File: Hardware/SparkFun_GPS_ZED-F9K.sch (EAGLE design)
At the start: 31 parts, among them J4 U.FL, Y1 32.768kHz

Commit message: Adds circuitry for active antenna or RF_IN
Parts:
- removed FRAME1: FRAME-LETTER, SparkFun-Aesthetics:FRAME-LETTER
- removed L2: 2.2uH, SparkFun-Coils:2.2μH_SHIELDED_INDUCTOR
- removed Y1: 32.768kHz, SparkFun-Clocks:CRYSTAL-32.768KHZSMD-3.2X1.5
- added D3: 24V, SparkFun-DiscreteSemi:DIODE_TVS
- added FRAME2: FRAME-LEDGER, SparkFun-Aesthetics:FRAME-LEDGER
- added J2: (no value), SparkFun-Connectors:USB_C2-LAYER
- added L1: 3.9NH, SparkFun-Coils:INDUCTOR-0402-3.9NH
- added Q1, Q2: 600mA/40V, SparkFun-DiscreteSemi:TRANS_PNP-MMBT4403
- added R6: 22, SparkFun-Resistors:22OHM-0402-1/10W-1%
- added R7: 10, SparkFun-Resistors:10OHM-0603-1/10W-5%
- added U1: UBLOX_ZED_F9K, classified:UBLOX_ZED_F9K
- C1: value 4.7uF -> 0.1uF; device SparkFun-Capacitors:4.7UF-0603-6.3V-(10%) -> SparkFun-Capacitors:0.1UF-0402-16V-10%
- C2: value 0.1uF -> 1.0uF; device SparkFun-Capacitors:0.1UF-0603-25V-(+80/-20%) -> SparkFun-Capacitors:1.0UF-0402-16V-10%
- FB1: value FERRITE_BEAD-120_OHM-0402 -> FERRITE_BEAD; device SparkFun-Coils:FERRITE_BEAD-120_OHM-0402 -> SparkFun-Coils:FERRITE_BEAD
- R5: value 10 -> 2.2KOHM-0402-1/16W-1%; device SparkFun-Resistors:10OHM-0603-1/10W-1% -> SparkFun-Resistors:2.2KOHM-0402-1/16W-1%
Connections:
- removed net ANT: FB1.1, J4.SIGNAL
- new net N$10: C1.1, L1.1, Q1.E
- new net N$11: Q2.E, R6.1
- new net N$5: C2.2, FB1.2, R6.2, R7.1
- new net N$6: Q1.B, Q2.C, R5.1
- new net N$7: C3.2, D3.C, J4.SIGNAL, L1.2
- new net RF_IN: C3.1, U1.RF_IN
- net 3.3V: now also FB1.1, U1.VCC; no longer R5.2
- net GND: now also C1.2, C2.1, D3.A, R5.2, U1.GND; no longer C3.2
- net N$9: now also Q1.C, Q2.B, R7.2; no longer C3.1, FB1.2, R5.1
- net V_BATT: now also U1.V_BKCP
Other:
- note added: "2.2K Ohm"
- note added: "VCC Range: 2.7V - 3.6V"
- note added: "ublox ZED-F9P"
- note added: "v01"
- note removed: "VCC Range: 1.89 - 3.6V"
- note removed: "uBlox ZOE-M8Q-0-10"
- note removed: "v10"
- moved on the sheet: B1, C1, C2, C3, D1, D2, FB1, J1, J3, J4, J5, JP1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

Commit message: Adds power circuitry with ESD protection, adds LEDs
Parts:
- removed JP4: JUMPER-SMT_2_NC_TRACE_SILK, SparkFun-Jumpers:JUMPER-SMT_2_NC_TRACE_SILK
- added C4, C5: 1.0uF, SparkFun-Capacitors:1.0UF-0603-16V-10%-X7R
- added C6: 1.0uF, SparkFun-Capacitors:1.0UF-0402-16V-10%
- added D4: PRTR5V0U2F, SparkFun-IC-Power:PRTR5V0U2F
- added D5, D6: BLUE, SparkFun-LED:LED-BLUE0603
- added J6: QWIIC_RIGHT_ANGLE, SparkFun-Connectors:QWIIC_CONNECTORJS-1MM
- added PPS, PWR, RTK: JUMPER-SMT_2_NC_TRACE_SILK, SparkFun-Jumpers:JUMPER-SMT_2_NC_TRACE_SILK
- added R10, R11: 27, SparkFun-Resistors:27OHM-0603-1/10W-1%
- added R12: 100K, SparkFun-Resistors:100KOHM-0402-1/16W-1%
- added R13, R14: 1KOHM-0402-1/16W-1%, SparkFun-Resistors:1KOHM-0402-1/16W-1%
- added R8, R9: 5.1k, SparkFun-Resistors:5.1KOHM5.1KOHM-0603-1/10W-1%
- added U2: 3.3V, SparkFun-IC-Power:V_REG_AP2112K-3.3V
- J1: value (none) -> QWIIC_RIGHT_ANGLE
- J5: device SparkFun-Connectors:CONN_041X04_NO_SILK -> SparkFun-Connectors:CONN_07
- R3, R4: value 2.2k -> 2.2K; device SparkFun-Resistors:2.2KOHM-0603-1/10W-1% -> SparkFun-Resistors:2.2KOHM-0402-1/16W-1%
- R5: value 2.2KOHM-0402-1/16W-1% -> 2.2K
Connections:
- removed net SDA/CS: J1.3, J3.8, R3.1
- removed net TIMEPULSE: J5.3
- new net DIR: J5.7, U1.DIR
- new net DMINUS: R11.2, U1.USB_D-
- new net DPLUS: R10.2, U1.USB_D+
- new net INT: U1.EXTINT
- new net N$14: J2.CC2, R8.2
- new net N$15: J2.CC1, R9.2
- new net N$16: D4.5, R10.1
- new net N$17: D4.4, R11.1
- new net N$20: D4.2, J2.D+
- new net N$21: D4.3, J2.D-
- new net N$22: R14.1, RTK.2
- new net N$23: PPS.2, R13.1
- new net N$24: D5.C, R13.2
- new net N$25: D6.C, R14.2
- new net PPS: D5.A, J5.3, U1.TIMEPULSE
- new net RTK_STAT: D6.A, U1.RTK_STAT
- new net RXI2: U1.RX2
- new net SDA/!CS: J1.3, J3.8, J6.3, R3.1, U1.SDA/!CS!
- new net SHLD: J2.SHLD
- new net TXO2: U1.TX2
- new net TX_READY: J5.5, U1.TX_READY
- new net VIN: D4.1, J2.VBUS, J3.4
- new net VOUT: C4.1, D4.6, U2.EN, U2.IN
- new net WT: J5.6, U1.WHEEL_TKS
- net !RESET: now also U1.!RESET!
- net !SAFEBOOT: now also U1.!SAFEBOOT!
- net 3.3V: now also C5.1, C6.1, D2.A, J6.2, R12.2, U1.V_USB, U2.OUT; no longer J3.4, R2.2
- net D_SEL: now also U1.D_SEL
- net GND: now also C4.2, C5.2, C6.2, J2.GND, J6.1, PPS.1, PWR.1, R12.1, R8.1, R9.1, RTK.1, U2.GND; no longer JP4.1
- net N$4: now also D2.C, R2.2; no longer D2.A, R2.1
- net N$8: now also PWR.2, R2.1; no longer D2.C, JP4.2
- net RXI/MOSI: now also U1.RX/MOSI
- net SCL/CLK: now also J6.4, U1.SCL/CLK
- net TXO/MISO: now also U1.TX/MISO
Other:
- note added: "!!!"
- note added: "1k"
- note added: "ADR Module - ublox ZED-F9P"
- note added: "Cut trace to disconnect respective LED"
- note added: "Order new parts"
- note added: "Power"
- note added: "VIN Range: 2.5V - 6V Max Current: 600mA"
- note removed: "Cut trace to disconnect LED"
- note removed: "ublox ZED-F9P"
- moved on the sheet: B1, C1, C2, C3, D1, D2, D3, FB1, J1, J2, J3, J4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

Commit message: Adds I/O protection to INPUTS using new part, removes active antenna circuitry in place of VCC bias for external patch active antennas
* Localizes parts into a rough shape for final product
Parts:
- removed C2: 1.0uF, SparkFun-Capacitors:1.0UF-0402-16V-10%
- removed C3: 47pF, SparkFun-Capacitors:47PF-0603-50V-5%
- removed D3: 24V, SparkFun-DiscreteSemi:DIODE_TVS
- removed FB1: FERRITE_BEAD, SparkFun-Coils:FERRITE_BEAD
- removed LOGO1: SFE_LOGO_NAME_FLAME.1_INCH, SparkFun-Aesthetics:SFE_LOGO_NAME_FLAME.1_INCH
- removed LOGO2: OSHW-LOGOS, SparkFun-Aesthetics:OSHW-LOGOS
- removed LOGO3: SFE_LOGO_FLAME.1_INCH, SparkFun-Aesthetics:SFE_LOGO_FLAME.1_INCH
- removed Q1, Q2: 600mA/40V, SparkFun-DiscreteSemi:TRANS_PNP-MMBT4403
- removed R6: 22, SparkFun-Resistors:22OHM-0402-1/10W-1%
- removed R7: 10, SparkFun-Resistors:10OHM-0603-1/10W-5%
- added U3: TRIPLE_BUFFER_74LVC3G07, classified:TRIPLE_BUFFER_74LVC3G07
- J5: device SparkFun-Connectors:CONN_07 -> SparkFun-Connectors:CONN_07NO_SILK
- L1: device SparkFun-Coils:INDUCTOR-0402-3.9NH -> SparkFun-Coils:FERRITE_BEAD-120_OHM-0402
- R5: value 2.2K -> 20; device SparkFun-Resistors:2.2KOHM-0402-1/16W-1% -> SparkFun-Resistors:20OHM-0603-1/10W-1%
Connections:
- removed net !INT: J5.1
- removed net !RESET: J5.2, U1.!RESET!
- removed net !SAFEBOOT: J5.4, U1.!SAFEBOOT!
- removed net INT: U1.EXTINT
- removed net N$10: C1.1, L1.1, Q1.E
- removed net N$11: Q2.E, R6.1
- removed net N$20: D4.2, J2.D+
- removed net N$21: D4.3, J2.D-
- removed net N$9: Q1.C, Q2.B, R7.2
- removed net VOUT: C4.1, D4.6, U2.EN, U2.IN
- new net !RESET_IN: U1.!RESET!, U3.1A
- new net !RESET_OUT: J5.2, U3.1Y
- new net !SAFEBOOT_IN: U1.!SAFEBOOT!, U3.3A
- new net !SAFEBOOT_OUT: J5.4, U3.3Y
- new net INT_IN: U1.EXTINT, U3.2A
- new net INT_OUT: J5.1, U3.2Y
- new net V_RF: R5.2, U1.V_RF
- new net V_USB: D4.1, J2.VBUS
- net 3.3V: now also U3.VCC; no longer FB1.1
- net DMINUS: now also R10.2; no longer R11.2
- net DPLUS: now also R11.2; no longer R10.2
- net GND: now also U3.GND; no longer C2.1, D3.A, R5.2
- net N$5: now also C1.1, L1.2, R5.1; no longer C2.2, FB1.2, R6.2, R7.1
- net N$6: now also D4.3, J2.D+; no longer Q1.B, Q2.C, R5.1
- net N$7: now also D4.2, J2.D-; no longer C3.2, D3.C, J4.SIGNAL, L1.2
- net RF_IN: now also J4.SIGNAL, L1.1; no longer C3.1
- net VIN: now also C4.1, D4.6, U2.EN, U2.IN; no longer D4.1, J2.VBUS
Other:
- note added: "I/O Buffer"
- note removed: "2.2K Ohm"
- moved on the sheet: C1, J3, J4, J5, R5

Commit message: Solidifies breakout board size
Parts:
- added J8: (no value), SparkFun-Connectors:CONN_09NO_SILK
- J3: device SparkFun-Connectors:CONN_08NO_SILK_FEMALE_PTH -> SparkFun-Connectors:CONN_06NO_SILK_NO_POP
- J5: device SparkFun-Connectors:CONN_07NO_SILK -> SparkFun-Connectors:CONN_06NO_SILK_NO_POP
- R2: value 1k -> 1KOHM-0402-1/16W-1%; device SparkFun-Resistors:1KOHM-0603-1/10W-1% -> SparkFun-Resistors:1KOHM-0402-1/16W-1%
- R8, R9: device SparkFun-Resistors:5.1KOHM5.1KOHM-0603-1/10W-1% -> SparkFun-Resistors:5.1KOHM-0402-1/16W-1%
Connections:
- new net !CS: J3.3
- new net SCK: J3.6
- net !RESET_OUT: now also J8.2; no longer J5.2
- net !SAFEBOOT_IN: now also J8.3
- net !SAFEBOOT_OUT: no longer J5.4
- net 3.3V: now also J8.7
- net DIR: no longer J5.7
- net GND: now also J3.1, J5.1, J8.6; no longer J3.6
- net INT_OUT: now also J8.4; no longer J5.1
- net PPS: now also J8.1; no longer J5.3
- net RXI/MOSI: now also J3.4; no longer J3.3
- net RXI2: now also J5.4
- net SCL/CLK: now also J8.9; no longer J3.7
- net SDA/!CS: now also J8.8; no longer J3.8
- net TXO/MISO: now also J3.5; no longer J3.2
- net TXO2: now also J5.5
- net TX_READY: now also J8.5; no longer J5.5
- net VIN: now also J3.2; no longer J3.4
- net WT: no longer J5.6

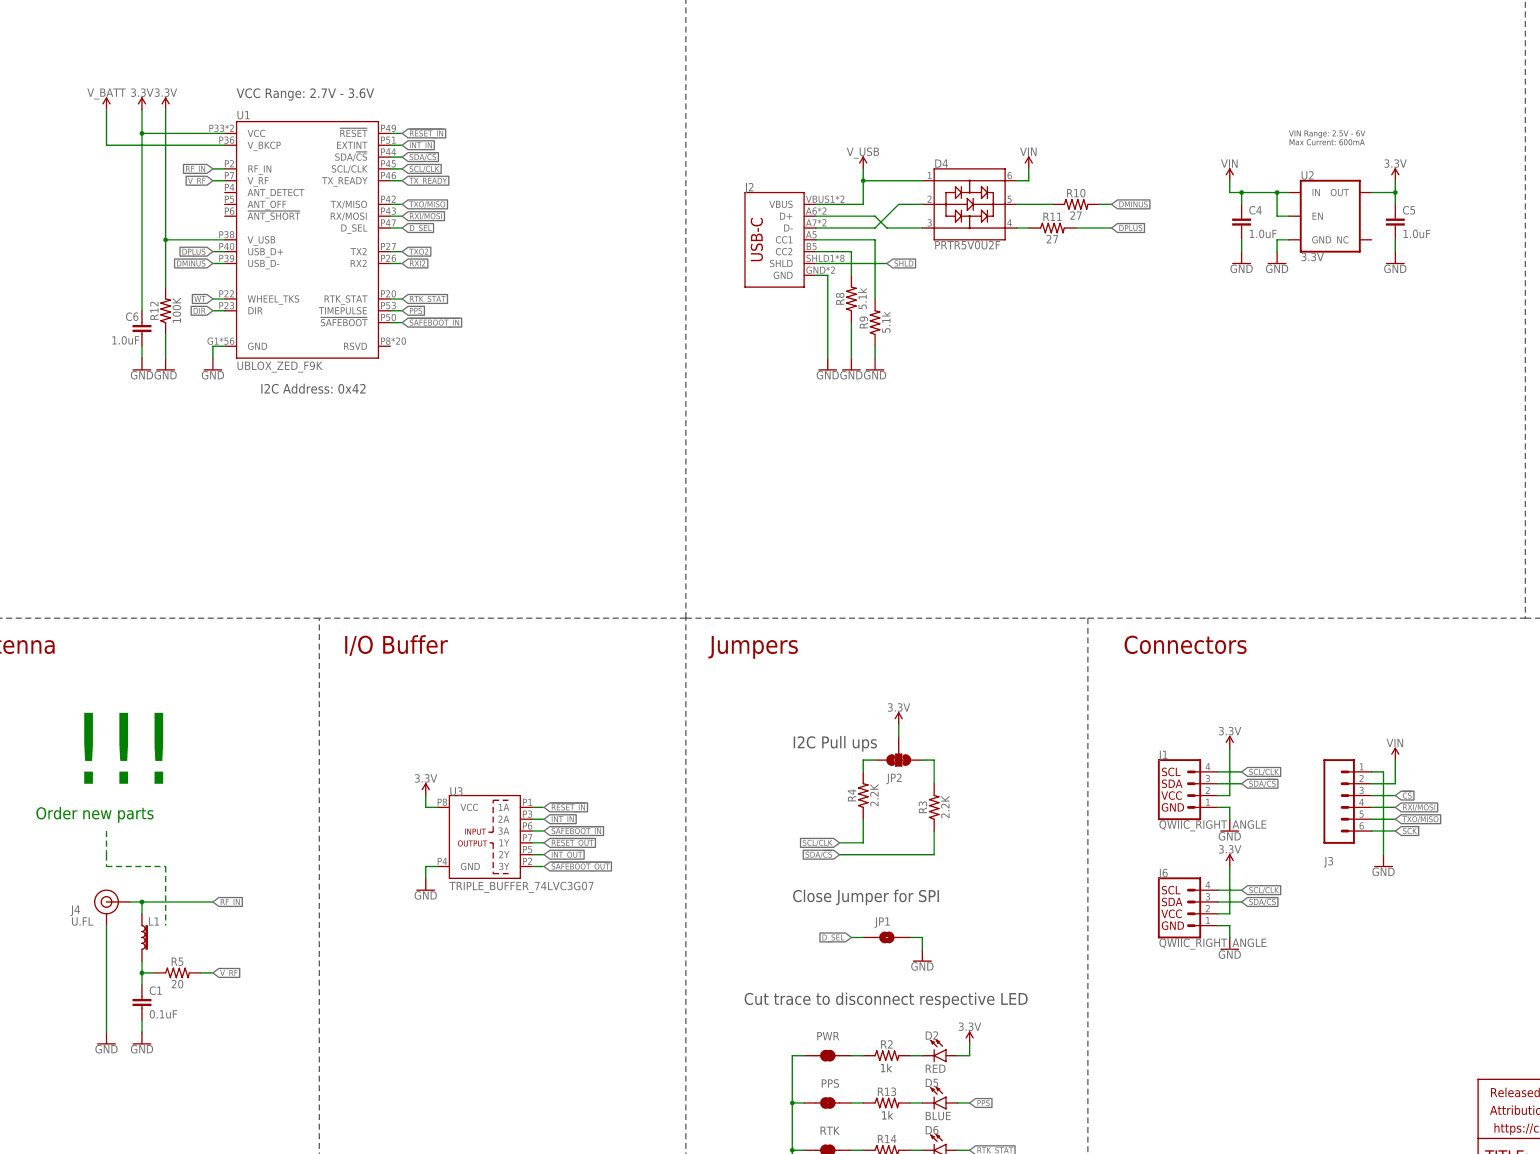
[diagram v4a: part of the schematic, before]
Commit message: Finalizes trace work for the Breakout board
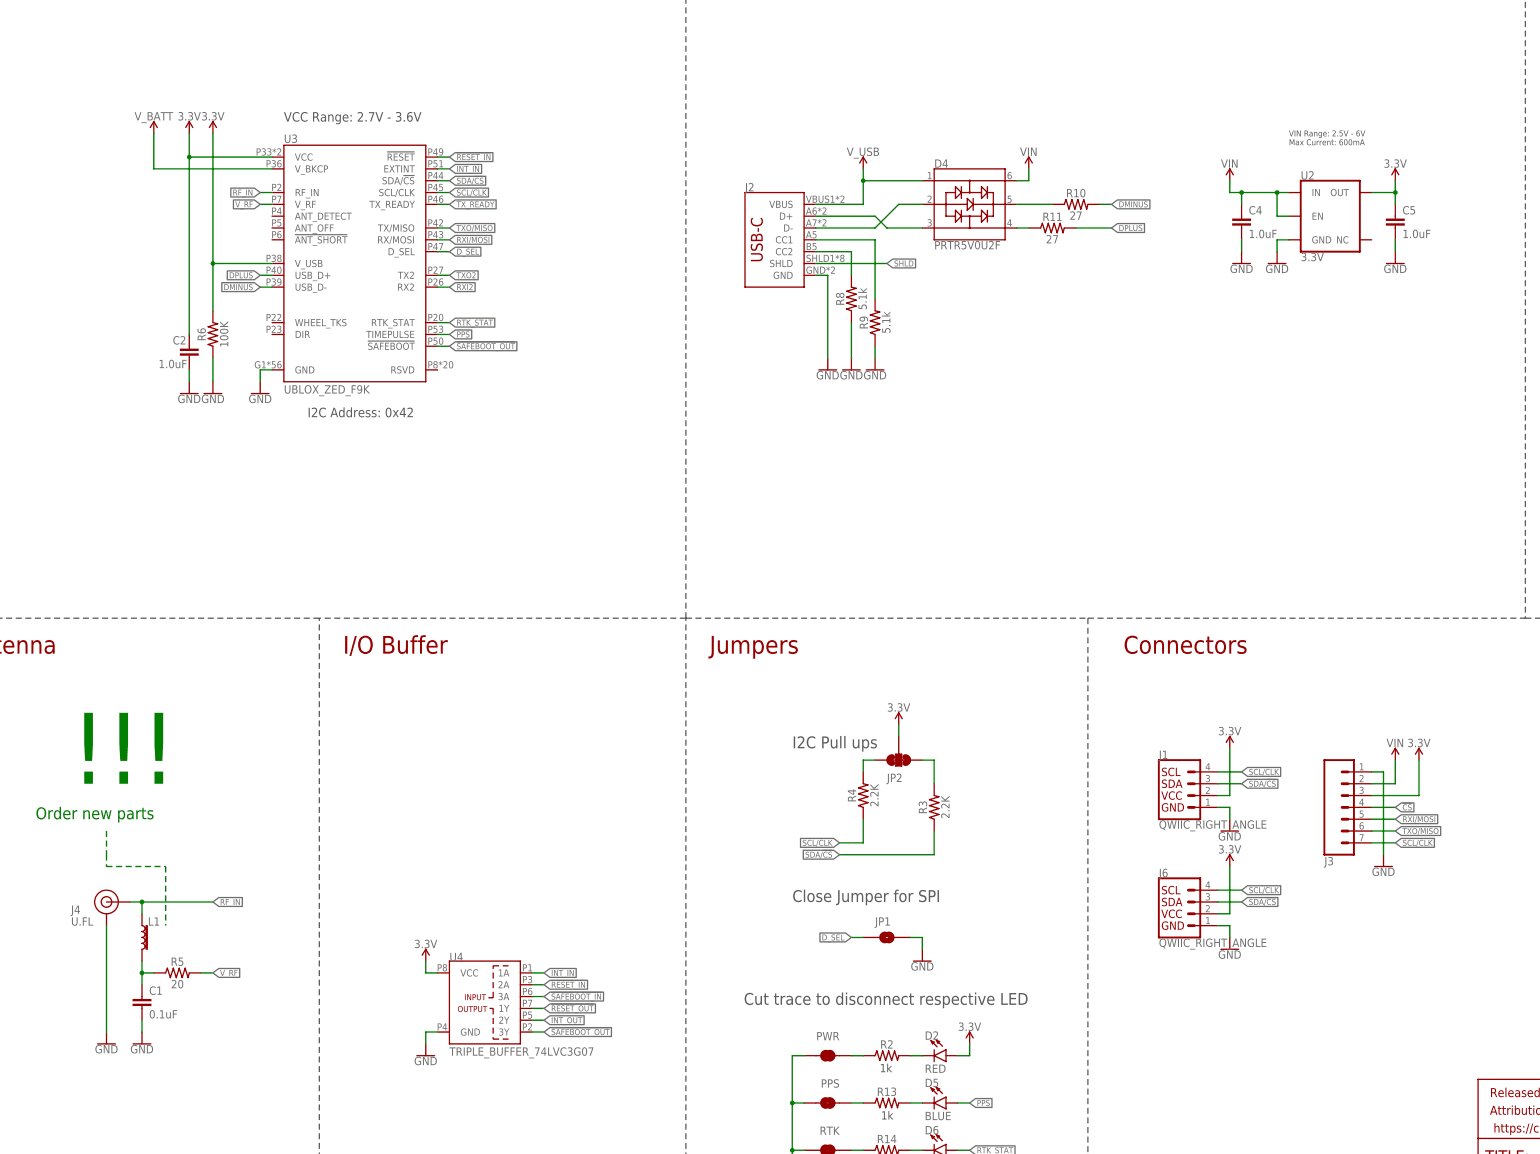
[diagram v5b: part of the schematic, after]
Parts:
- removed C6: 1.0uF, SparkFun-Capacitors:1.0UF-0402-16V-10%
- removed R12: 100K, SparkFun-Resistors:100KOHM-0402-1/16W-1%
- removed U1: UBLOX_ZED_F9K, classified:UBLOX_ZED_F9K
- added C2: 1.0uF, SparkFun-Capacitors:1.0UF-0402-16V-10%
- added R6: 100K, SparkFun-Resistors:100KOHM-0402-1/16W-1%
- added U4: TRIPLE_BUFFER_74LVC3G07, classified:TRIPLE_BUFFER_74LVC3G07
- J3: device SparkFun-Connectors:CONN_06NO_SILK_NO_POP -> SparkFun-Connectors:CONN_07NO_SILK
- U3: value TRIPLE_BUFFER_74LVC3G07 -> UBLOX_ZED_F9K; device classified:TRIPLE_BUFFER_74LVC3G07 -> classified:UBLOX_ZED_F9K
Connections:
- removed net DIR: U1.DIR
- removed net SCK: J3.6
- removed net WT: U1.WHEEL_TKS
- net !CS: now also J3.4; no longer J3.3
- net !RESET_IN: now also U3.!RESET!, U4.2A; no longer U1.!RESET!, U3.1A
- net !RESET_OUT: now also U4.1Y; no longer U3.1Y
- net !SAFEBOOT_IN: now also U4.3A; no longer U1.!SAFEBOOT!, U3.3A
- net !SAFEBOOT_OUT: now also U3.!SAFEBOOT!, U4.3Y; no longer U3.3Y
- net 3.3V: now also C2.1, J3.3, R6.2, U3.V_USB, U4.VCC; no longer C6.1, R12.2, U1.VCC, U1.V_USB
- net DMINUS: now also U3.USB_D-; no longer U1.USB_D-
- net DPLUS: now also U3.USB_D+; no longer U1.USB_D+
- net D_SEL: now also U3.D_SEL; no longer U1.D_SEL
- net GND: now also C2.2, R6.1, U4.GND; no longer C6.2, R12.1, U1.GND
- net INT_IN: now also U3.EXTINT, U4.1A; no longer U1.EXTINT, U3.2A
- net INT_OUT: now also U4.2Y; no longer U3.2Y
- net PPS: now also U3.TIMEPULSE; no longer U1.TIMEPULSE
- net RF_IN: now also U3.RF_IN; no longer U1.RF_IN
- net RTK_STAT: now also U3.RTK_STAT; no longer U1.RTK_STAT
- net RXI/MOSI: now also J3.5, U3.RX/MOSI; no longer J3.4, U1.RX/MOSI
- net RXI2: now also U3.RX2; no longer U1.RX2
- net SCL/CLK: now also J3.7, U3.SCL/CLK; no longer U1.SCL/CLK
- net SDA/!CS: now also U3.SDA/!CS!; no longer U1.SDA/!CS!
- net TXO/MISO: now also J3.6, U3.TX/MISO; no longer J3.5, U1.TX/MISO
- net TXO2: now also U3.TX2; no longer U1.TX2
- net TX_READY: now also U3.TX_READY; no longer U1.TX_READY
- net V_BATT: now also U3.V_BKCP; no longer U1.V_BKCP
- net V_RF: now also U3.V_RF; no longer U1.V_RF

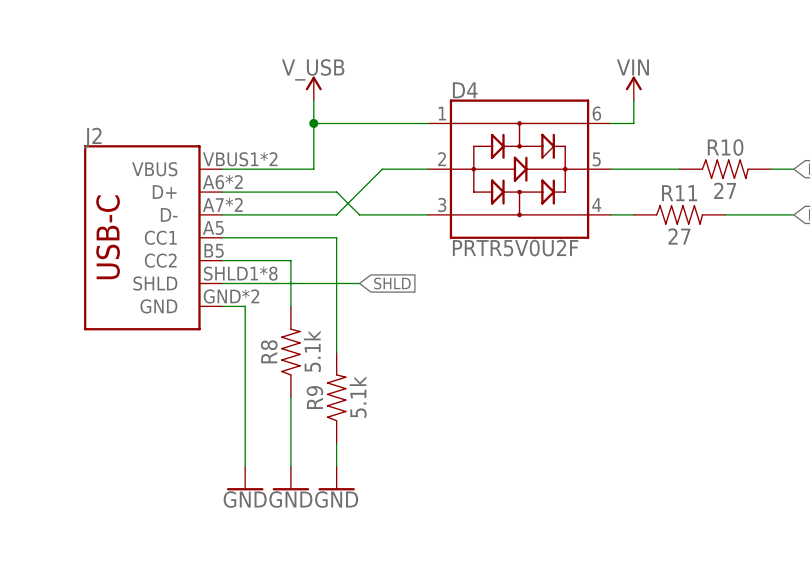
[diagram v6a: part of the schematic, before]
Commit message: More work to ground pour
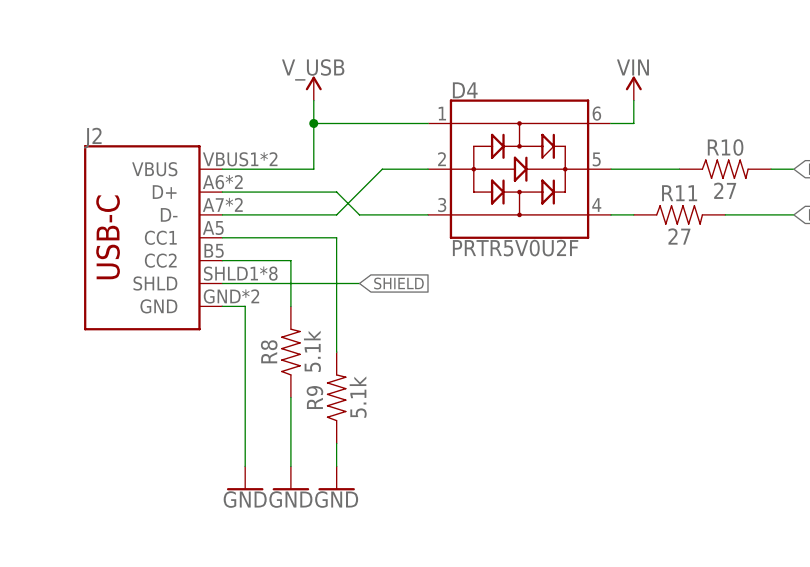
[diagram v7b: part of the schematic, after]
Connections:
- net SHLD renamed SHIELD
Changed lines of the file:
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@@
 </segment>
 </net>
-<net name="SHLD" class="0">
+<net name="SHIELD" class="0">
 <segment>
 <pinref part="J2" gate="J1" pin="SHLD"/>

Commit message: Adds labels to breakout board
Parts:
- added LOGO1: SFE_LOGO_NAME_FLAME.2_INCH, SparkFun-Aesthetics:SFE_LOGO_NAME_FLAME.2_INCH
- added LOGO2: QWIIC_LOGO_4MM, SparkFun-Aesthetics:QWIIC_LOGO_4MM
- added LOGO3: OSHW-LOGOM, SparkFun-Aesthetics:OSHW-LOGOM
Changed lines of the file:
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@@
 <?xml version="1.0" encoding="utf-8"?>
 <!DOCTYPE eagle SYSTEM "eagle.dtd">
-<eagle version="9.5.2">
+<eagle version="9.5.1">
 <drawing>
 <settings>
@@
 <part name="GND22" library="SparkFun-PowerSymbols" deviceset="GND" device=""/>
 <part name="SUPPLY2" library="SparkFun-PowerSymbols" deviceset="3.3V" device=""/>
+<part name="LOGO1" library="SparkFun-Aesthetics" deviceset="SFE_LOGO_NAME_FLAME" device=".2_INCH"/>
+<part name="LOGO2" library="SparkFun-Aesthetics" deviceset="QWIIC_LOGO" device="_4MM"/>
+<part name="LOGO3" library="SparkFun-Aesthetics" deviceset="OSHW-LOGO" device="M"/>
 </parts>
 <sheets>
@@
 <attribute name="VALUE" x="317.5" y="106.934" size="1.778" layer="96" align="bottom-center"/>
 </instance>
+<instance part="LOGO1" gate="G$1" x="373.38" y="33.02" smashed="yes"/>
+<instance part="LOGO2" gate="G$1" x="358.14" y="40.64" smashed="yes"/>
+<instance part="LOGO3" gate="G$1" x="332.74" y="45.72" smashed="yes"/>
 </instances>
 <busses>
@@
 </nets>
 </sheet>
+<sheet>
+<plain>
+</plain>
+<instances>
+</instances>
+<busses>
+</busses>
+<nets>
+</nets>
+</sheet>
+<sheet>
+<plain>
+</plain>
+<instances>
+</instances>
+<busses>
+</busses>
+<nets>
+</nets>
+</sheet>
+<sheet>
+<plain>
+</plain>
+<instances>
+</instances>
+<busses>
+</busses>
+<nets>
+</nets>
+</sheet>
+<sheet>
+<plain>
+</plain>
+<instances>
+</instances>
+<busses>
+</busses>
+<nets>
+</nets>
+</sheet>
